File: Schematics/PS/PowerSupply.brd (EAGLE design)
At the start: 99.1 x 76.2 mm, 22 parts

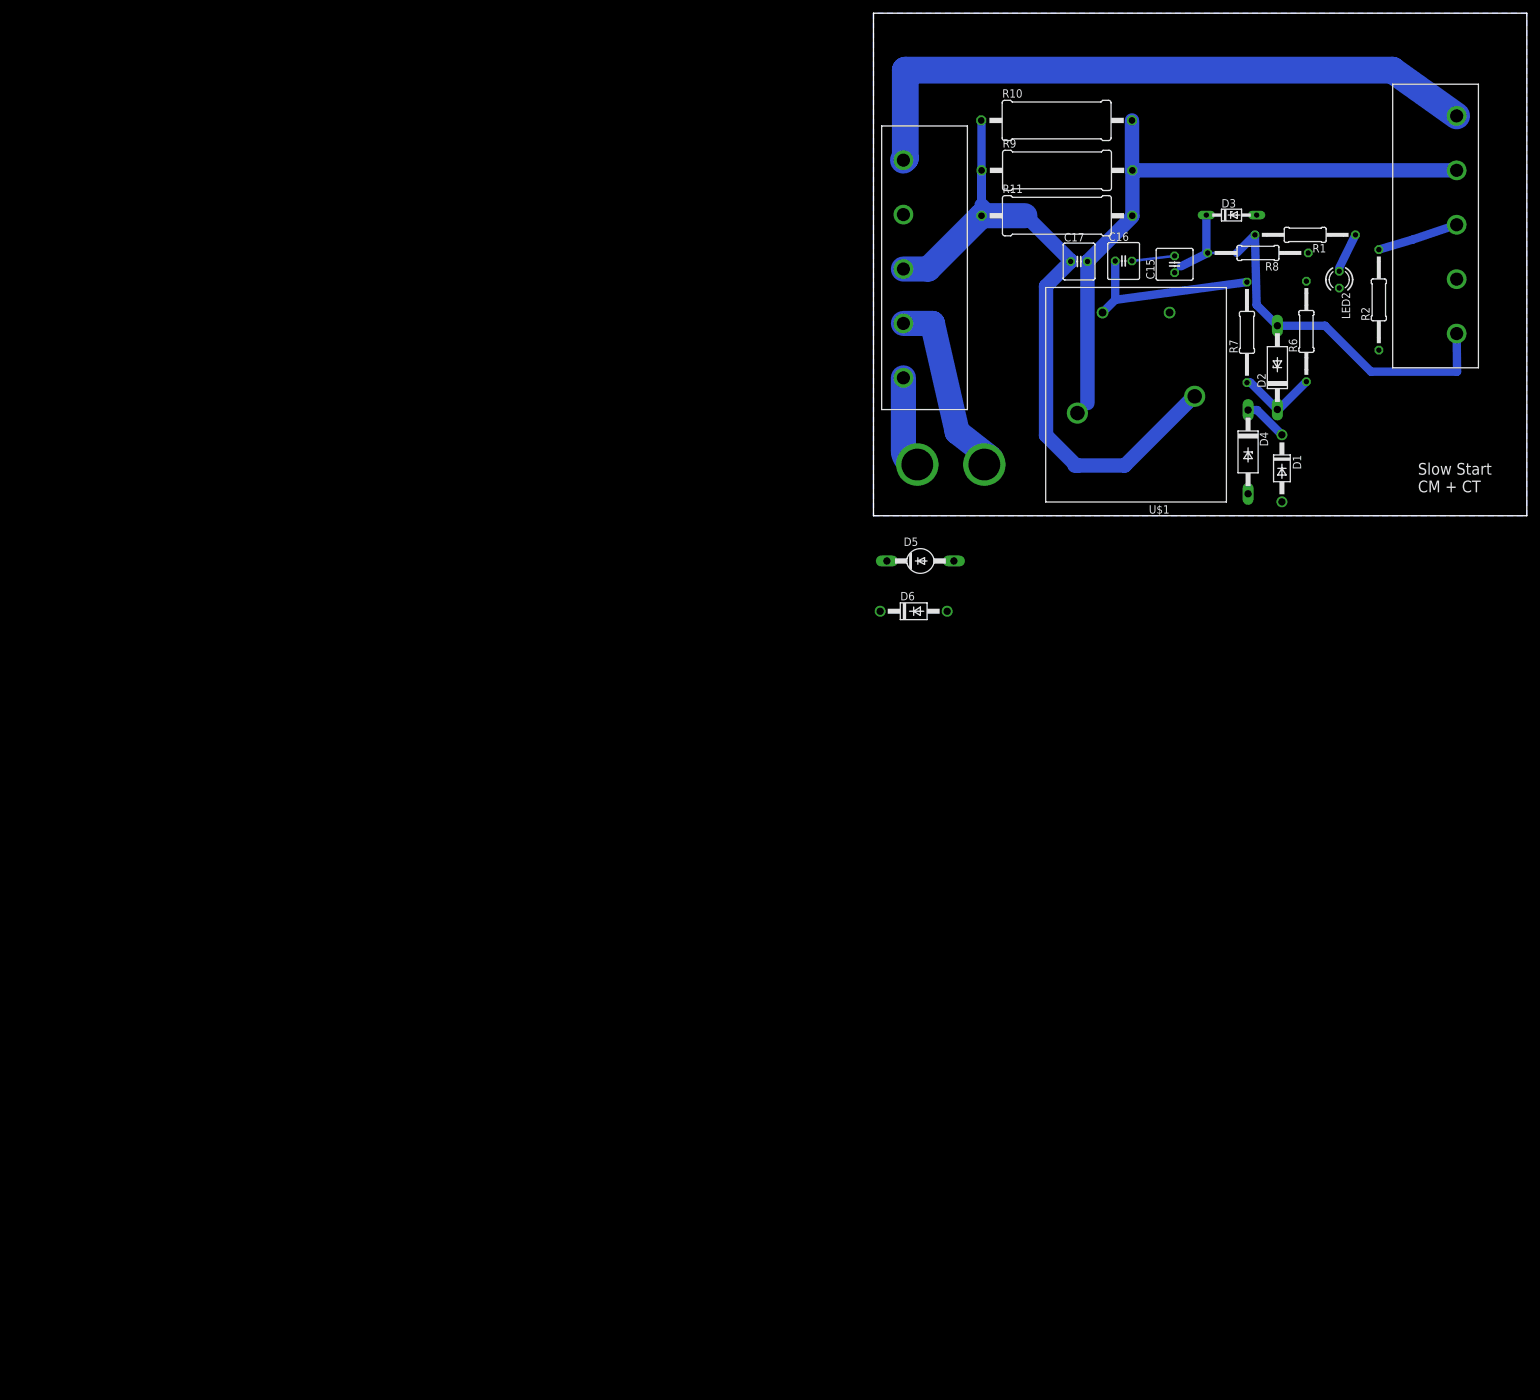
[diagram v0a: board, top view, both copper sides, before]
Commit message: added new power supply schem and did some file cleanup
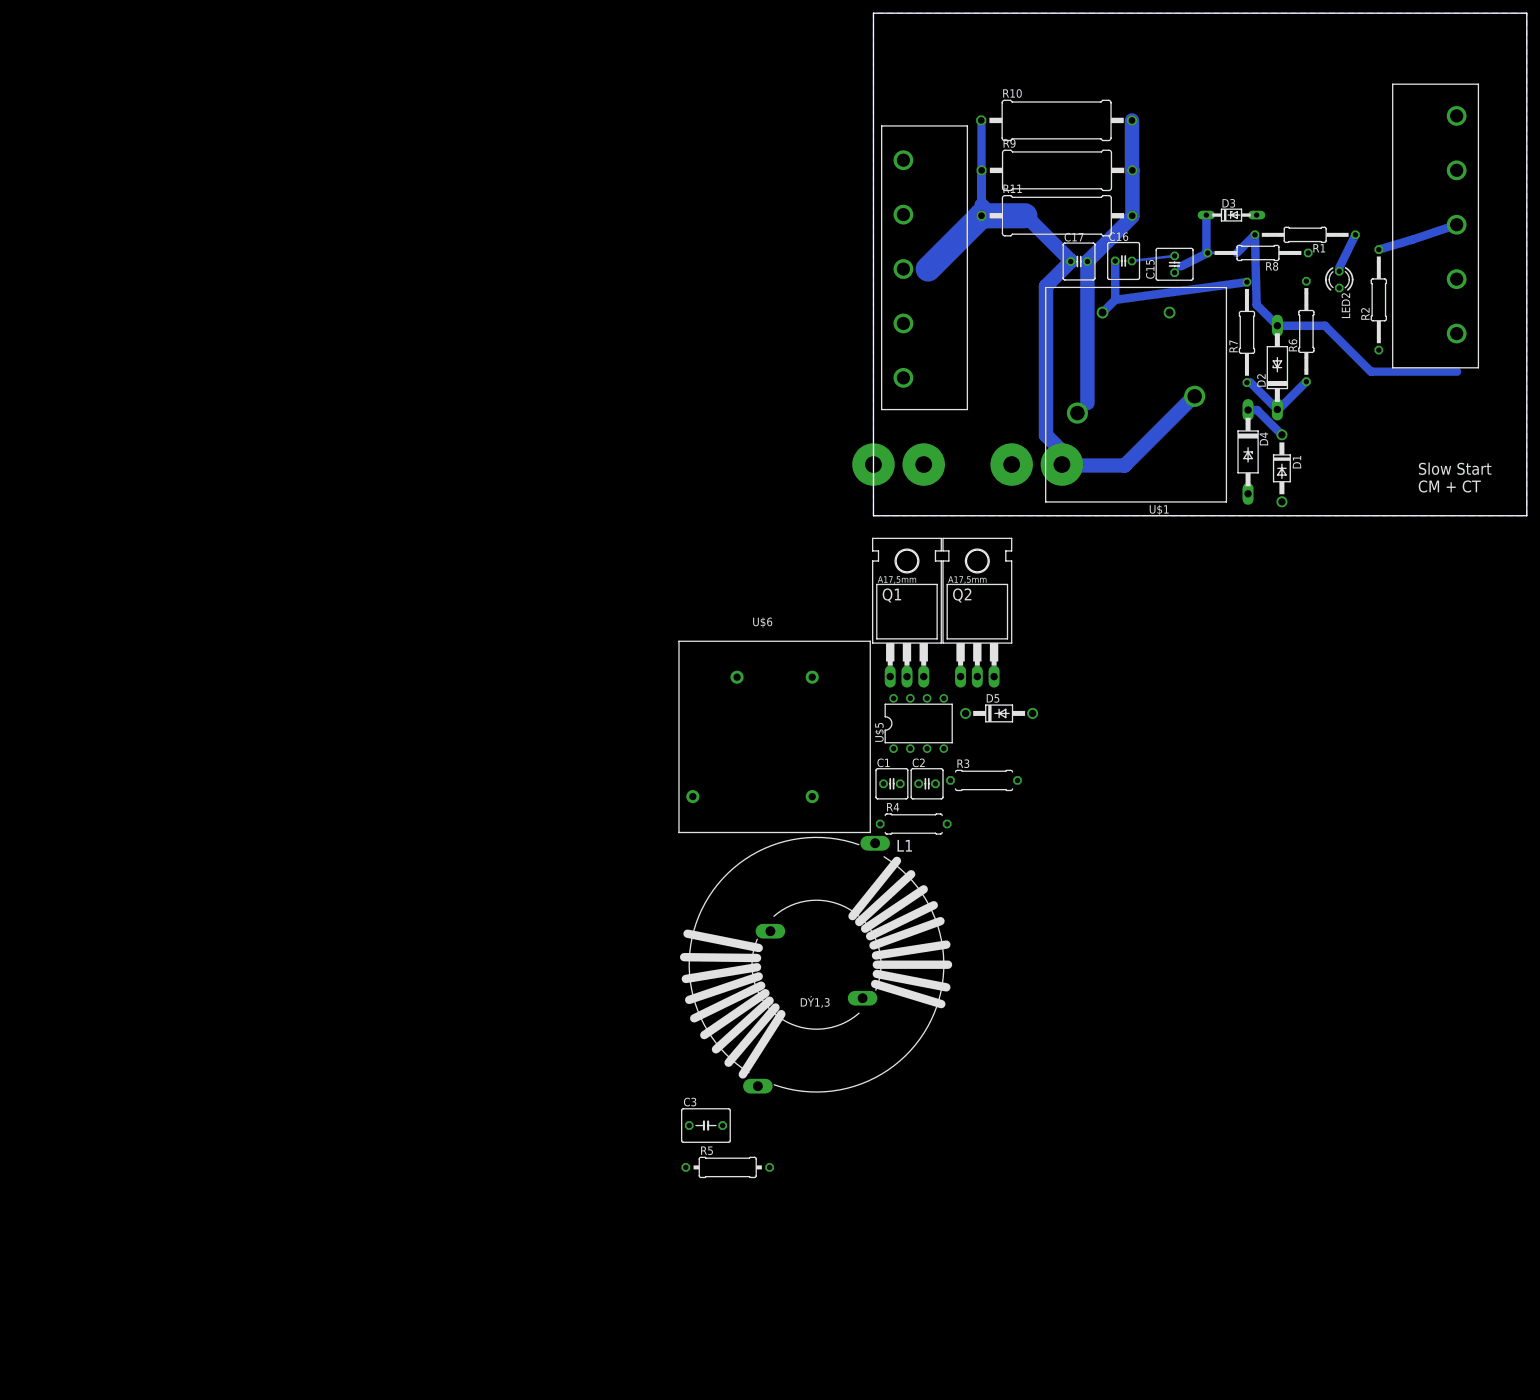
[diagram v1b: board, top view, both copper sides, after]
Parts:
- removed D6: 1N4004, T06_LockBox:DO41-10
- added C1, C2: (no value), resistor:C025-050X050
- added C3: (no value), resistor:C050-050X075
- added L1: RKZ4, inductors:RKZ4
- added Q1, Q2: BUZ10, transistor-fet:TO220
- added R3, R4: (no value), resistor:0309/10
- added R5: (no value), resistor:0309/12
- added U$5: IRS2153D, Amplifier_Parts:IRS2153D
- added U$6: GBPC3510W, Amplifier_Parts:GBPC3510W
- D5: value BYV12 -> 1N4933; device diode:SGA-10 -> diode:DO41-10
- moved D5 26.0 mm to (19.1, -30.0)
- moved U$4 11.8 mm to (23.5, 7.76)
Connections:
- removed net VAC+: U$2.P$4, U$3.P$6
- new net N$13: C1.1, U$5.4
- new net N$14: C2.1, U$5.6
- new net N$15: L1.E1, U$2.P$6
- new net N$16: L1.E2, U$2.P$4
- new net N$17: L1.A1, U$6.AC1
- new net N$18: L1.A2, U$6.AC2
- new net N$4: D5.A, R4.1, U$5.1
- new net N$6: C2.2, D5.C, U$5.8
- new net N$7: C1.2, R3.1, U$5.3
- new net N$9: R3.2, U$5.2
- new net PE: U$2.P$5
- net GND: no longer U$2.P$2
- net N$12: no longer U$3.P$4
- net N$2: now also U$2.P$2, U$4.P$1, U$4.P$3; no longer U$2.P$6, U$4.P$2
- net N$5: now also U$2.P$3, U$4.P$2, U$4.P$4; no longer U$2.P$5, U$4.P$1
- net N$8: no longer U$3.P$5
- net VAC-: no longer U$2.P$3
- net VCC: now also U$3.P$2
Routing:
- net VAC+: track 99.6 -> 0.00 mm
- net N$8: track 97.0 -> 47.9 mm
- net N$5: track 29.1 -> 0.00 mm
- net N$2: track 14.0 -> 0.00 mm
- net N$12: track 71.0 -> 65.2 mm
- net VAC-: track 125.4 -> 121.6 mm
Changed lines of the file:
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@@
 <element name="R1" library="resistor" package="0207/15" value="10k" x="65.4601" y="42.5909625" rot="R180"/>
 <element name="R2" library="resistor" package="0207/15" value="100" x="76.623821875" y="32.736103125" rot="R90"/>
-<element name="U$4" library="Amplifier_Parts" package="FUSE_PADS" value="FUSE" x="11.7266" y="7.763428125" rot="R180"/>
+<element name="U$4" library="Amplifier_Parts" package="FUSE_PADS" value="FUSE" x="23.495" y="7.763428125" rot="R180"/>
 <element name="U$2" library="Amplifier_Parts" package="SCREW_TERMINAL_5" value="SCREW_TERMINAL_5" x="2.54" y="38.1" rot="R270"/>
 <element name="U$3" library="Amplifier_Parts" package="SCREW_TERMINAL_5" value="SCREW_TERMINAL_5" x="90.424" y="43.434" rot="R90"/>
-<element name="D5" library="diode" package="SGA-10" value="BYV12" x="7.112" y="-6.858"/>
-<element name="D6" library="T06_LockBox" package="DO41-10" value="1N4004" x="6.096" y="-14.478"/>
+<element name="U$5" library="Amplifier_Parts" package="IRS2153D" value="IRS2153D" x="6.858" y="-31.496"/>
+<element name="D5" library="diode" package="DO41-10" value="1N4933" x="19.05" y="-29.972"/>
+<element name="R3" library="resistor" package="0309/10" value="" x="16.764" y="-40.132"/>
+<element name="R4" library="resistor" package="0309/10" value="" x="6.096" y="-46.736"/>
+<element name="C1" library="resistor" package="C025-050X050" value="" x="2.794" y="-40.64"/>
+<element name="C2" library="resistor" package="C025-050X050" value="" x="8.128" y="-40.64"/>
+<element name="Q1" library="transistor-fet" package="TO220" value="BUZ10" x="5.08" y="-18.034"/>
+<element name="Q2" library="transistor-fet" package="TO220" value="BUZ10" x="15.748" y="-18.034"/>
+<element name="U$6" library="Amplifier_Parts" package="GBPC3510W" value="GBPC3510W" x="-16.256" y="-28.448"/>
+<element name="L1" library="inductors" package="RKZ4" value="RKZ4" x="-8.636" y="-68.072"/>
+<element name="C3" library="resistor" package="C050-050X075" value="" x="-25.4" y="-92.456"/>
+<element name="R5" library="resistor" package="0309/12" value="" x="-22.098" y="-98.806"/>
 </elements>
 <signals>
@@
 <vertex x="0" y="76.2"/>
 </polygon>
-<contactref element="U$2" pad="P$2"/>
 <contactref element="C16" pad="2"/>
 <contactref element="D4" pad="A"/>
@@
 <contactref element="R2" pad="1"/>
 <wire x1="45.658725" y1="39.39528125" x2="39.19525625" y2="38.629" width="0.381" layer="16"/>
+<wire x1="70.620678125" y1="34.528765625" x2="65.917503125" y2="39.844834375" width="0" layer="19" extent="1-1"/>
+<wire x1="58.09415" y1="45.591403125" x2="65.917503125" y2="39.844834375" width="0" layer="19" extent="1-1"/>
+<wire x1="76.623821875" y1="25.116103125" x2="70.620678125" y2="34.528765625" width="0" layer="19" extent="1-1"/>
+<wire x1="45.658725" y1="39.39528125" x2="58.09415" y2="45.591403125" width="0" layer="19" extent="1-1"/>
+<wire x1="44.892303125" y1="30.808921875" x2="45.658725" y2="39.39528125" width="0" layer="19" extent="1-1"/>
+<wire x1="61.9296125" y1="2.109978125" x2="76.623821875" y2="25.116103125" width="0" layer="19" extent="1-1"/>
+<wire x1="56.795371875" y1="3.327840625" x2="61.9296125" y2="2.109978125" width="0" layer="19" extent="1-1"/>
 </signal>
 <signal name="VCC">
 <contactref element="R6" pad="2"/>
+<contactref element="U$3" pad="P$2"/>
+<wire x1="65.637840625" y1="35.564825" x2="88.424" y2="35.874" width="0" layer="19" extent="1-1"/>
 </signal>
 <signal name="VAC-">
@@
 <contactref element="C17" pad="1"/>
 <contactref element="U$1" pad="COM"/>
-<contactref element="U$2" pad="P$3"/>
-<wire x1="4.54" y1="37.41" x2="8.298521875" y2="37.41" width="3.81" layer="16"/>
 <wire x1="8.298521875" y1="37.41" x2="16.37845" y2="45.489928125" width="3.81" layer="16"/>
 <wire x1="16.37845" y1="45.489928125" x2="16.37845" y2="59.8991" width="1.27" layer="16"/>
@@
 <contactref element="C17" pad="2"/>
 <contactref element="U$1" pad="NO"/>
-<contactref element="U$3" pad="P$5"/>
 <wire x1="39.196828125" y1="59.940721875" x2="39.196828125" y2="52.427915625" width="2.1844" layer="16"/>
 <wire x1="39.196828125" y1="52.427915625" x2="39.257265625" y2="52.367478125" width="1.27" layer="16"/>
@@
 <wire x1="32.4429" y1="38.54859375" x2="32.4429" y2="17.08951875" width="2.1844" layer="16"/>
 <wire x1="32.4429" y1="17.08951875" x2="30.922303125" y2="15.568921875" width="0.4064" layer="16"/>
-<wire x1="88.424" y1="52.374" x2="39.257265625" y2="52.374" width="2.1844" layer="16"/>
 <wire x1="39.257265625" y1="52.374" x2="39.257265625" y2="52.367478125" width="2.1844" layer="16"/>
 </signal>
@@
 <contactref element="C15" pad="1"/>
 <contactref element="R1" pad="2"/>
-<contactref element="U$3" pad="P$4"/>
 <wire x1="50.677503125" y1="39.844834375" x2="46.616278125" y2="37.812834375" width="1.27" layer="16"/>
 <wire x1="46.616278125" y1="37.812834375" x2="45.658725" y2="36.85528125" width="0.4064" layer="16"/>
@@
 <wire x1="68.468728125" y1="28.813271875" x2="75.438" y2="21.844" width="1.27" layer="16"/>
 <wire x1="75.438" y1="21.844" x2="88.486" y2="21.844" width="1.27" layer="16"/>
-<wire x1="88.486" y1="21.844" x2="88.424" y2="27.624" width="1.27" layer="16"/>
 <wire x1="50.677503125" y1="39.844834375" x2="55.093971875" y2="39.844834375" width="0.381" layer="16"/>
 <wire x1="55.093971875" y1="39.844834375" x2="57.8401" y2="42.5909625" width="1.27" layer="16"/>
 <wire x1="50.47415" y1="45.591403125" x2="50.47415" y2="40.0481875" width="1.27" layer="16"/>
 <wire x1="50.47415" y1="40.0481875" x2="50.677503125" y2="39.844834375" width="0.381" layer="16"/>
-</signal>
-<signal name="VAC+">
-<contactref element="U$2" pad="P$4"/>
-<contactref element="U$3" pad="P$6"/>
-<wire x1="4.54" y1="53.91" x2="4.826" y2="54.196" width="4.064" layer="16"/>
-<wire x1="4.826" y1="54.196" x2="4.826" y2="67.564" width="4.064" layer="16"/>
-<wire x1="4.826" y1="67.564" x2="78.69" y2="67.564" width="4.064" layer="16"/>
-<wire x1="78.69" y1="67.564" x2="88.424" y2="60.624" width="4.064" layer="16"/>
-</signal>
-<signal name="N$2">
-<contactref element="U$4" pad="P$2"/>
-<contactref element="U$2" pad="P$6"/>
-<wire x1="4.54" y1="20.91" x2="4.54" y2="9.870028125" width="3.81" layer="16"/>
-<wire x1="4.54" y1="9.870028125" x2="6.6466" y2="7.763428125" width="3.81" layer="16" curve="90"/>
-</signal>
-<signal name="N$5">
-<contactref element="U$2" pad="P$5"/>
-<contactref element="U$4" pad="P$1"/>
-<wire x1="4.54" y1="29.16" x2="8.94" y2="29.16" width="3.81" layer="16"/>
-<wire x1="8.94" y1="29.16" x2="12.7" y2="12.7" width="3.81" layer="16"/>
-<wire x1="12.7" y1="12.7" x2="17.78" y2="8.736828125" width="3.81" layer="16"/>
-<wire x1="17.78" y1="8.736828125" x2="16.8066" y2="7.763428125" width="0.4064" layer="16"/>
 </signal>
 <signal name="N$1">
@@
 <wire x1="81.777896875" y1="41.880103125" x2="88.424" y2="44.124" width="1.27" layer="16"/>
 </signal>
+<signal name="N$4">
+<contactref element="D5" pad="A"/>
+<contactref element="U$5" pad="1"/>
+<contactref element="R4" pad="1"/>
+<wire x1="3.048" y1="-35.306" x2="1.016" y2="-46.736" width="0" layer="19" extent="1-1"/>
+<wire x1="24.13" y1="-29.972" x2="3.048" y2="-35.306" width="0" layer="19" extent="1-1"/>
+</signal>
+<signal name="N$6">
+<contactref element="D5" pad="C"/>
+<contactref element="U$5" pad="8"/>
+<contactref element="C2" pad="2"/>
+<wire x1="13.97" y1="-29.972" x2="9.398" y2="-40.64" width="0" layer="19" extent="1-1"/>
+<wire x1="3.048" y1="-27.686" x2="13.97" y2="-29.972" width="0" layer="19" extent="1-1"/>
+</signal>
+<signal name="N$7">
+<contactref element="R3" pad="1"/>
+<contactref element="C1" pad="2"/>
+<contactref element="U$5" pad="3"/>
+<wire x1="8.128" y1="-35.306" x2="4.064" y2="-40.64" width="0" layer="19" extent="1-1"/>
+<wire x1="11.684" y1="-40.132" x2="8.128" y2="-35.306" width="0" layer="19" extent="1-1"/>
+</signal>
+<signal name="N$9">
+<contactref element="U$5" pad="2"/>
+<contactref element="R3" pad="2"/>
+<wire x1="21.844" y1="-40.132" x2="5.588" y2="-35.306" width="0" layer="19" extent="1-1"/>
+</signal>
+<signal name="N$13">
+<contactref element="U$5" pad="4"/>
+<contactref element="C1" pad="1"/>
+<wire x1="10.668" y1="-35.306" x2="1.524" y2="-40.64" width="0" layer="19" extent="1-1"/>
+</signal>
+<signal name="N$14">
+<contactref element="C2" pad="1"/>
+<contactref element="U$5" pad="6"/>
+<wire x1="8.128" y1="-27.686" x2="6.858" y2="-40.64" width="0" layer="19" extent="1-1"/>
+</signal>
+<signal name="N$2">
+<contactref element="U$2" pad="P$2"/>
+<contactref element="U$4" pad="P$1"/>
+<contactref element="U$4" pad="P$3"/>
+<wire x1="20.955" y1="7.763428125" x2="4.54" y2="45.66" width="0" layer="19" extent="1-1"/>
+<wire x1="28.575" y1="7.763428125" x2="20.955" y2="7.763428125" width="0" layer="19" extent="1-1"/>
+</signal>
+<signal name="N$5">
+<contactref element="U$4" pad="P$2"/>
+<contactref element="U$4" pad="P$4"/>
+<contactref element="U$2" pad="P$3"/>
+<wire x1="7.62" y1="7.763428125" x2="4.54" y2="37.41" width="0" layer="19" extent="1-1"/>
+<wire x1="0" y1="7.763428125" x2="7.62" y2="7.763428125" width="0" layer="19" extent="1-1"/>
+</signal>
+<signal name="PE">
+<contactref element="U$2" pad="P$5"/>
+</signal>
+<signal name="N$15">
+<contactref element="U$2" pad="P$6"/>
+<contactref element="L1" pad="E1"/>
+<wire x1="4.54" y1="20.91" x2="-1.651" y2="-73.152" width="0" layer="19" extent="1-1"/>
+</signal>
+<signal name="N$16">
+<contactref element="L1" pad="E2"/>
+<contactref element="U$2" pad="P$4"/>
+<wire x1="4.54" y1="53.91" x2="-15.621" y2="-62.992" width="0" layer="19" extent="1-1"/>
+</signal>
+<signal name="N$17">
+<contactref element="L1" pad="A1"/>
+<contactref element="U$6" pad="AC1"/>
+<wire x1="-9.286" y1="-24.478" x2="0.254" y2="-49.657" width="0" layer="19" extent="1-1"/>
+</signal>
+<signal name="N$18">
+<contactref element="U$6" pad="AC2"/>
+<contactref element="L1" pad="A2"/>
+<wire x1="-27.386" y1="-42.578" x2="-17.526" y2="-86.487" width="0" layer="19" extent="1-1"/>
+</signal>
 </signals>

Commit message: updates to PS schematic
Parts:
- removed Q1, Q2: BUZ10, transistor-fet:TO220
- added C4: (no value), resistor:C025-050X050
- added D6, D7: 1N4933, diode:DO41-10
- added R12: (no value), resistor:0617/22
- added R13, R14: (no value), resistor:0204V
- added T1, T2: IRFP240, Amplifier_Parts:IRFP240
- added TRAFO1: COIL_FORMER, Amplifier_Parts:COIL_FORMER
- R5: device resistor:0309/12 -> resistor:0617/22
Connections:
- removed net N$13 (its old number): C1.1, U$5.4
- new net N$19: D6.C, R13.2, T1.G
- new net N$20: D7.A, R14.1, U$5.5
- new net N$21: D7.C, R14.2, T2.G
- new net N$22: C2.1, T1.S, T2.D, TRAFO1.P$1, U$5.6
- new net N$9: C4.2, D5.A, R4.1, U$5.1
- net N$14: now also D6.A, R13.1, U$5.7; no longer C2.1, U$5.6
- net N$4: now also C3.1, R12.2, R4.2, R5.2, U$6.V+; no longer D5.A, R4.1, U$5.1
- net PE: now also C1.1, C3.2, C4.1, R12.1, R5.1, TRAFO1.P$5, TRAFO1.P$6, U$5.4, U$6.V-
